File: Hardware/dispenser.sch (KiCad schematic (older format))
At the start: 5 parts

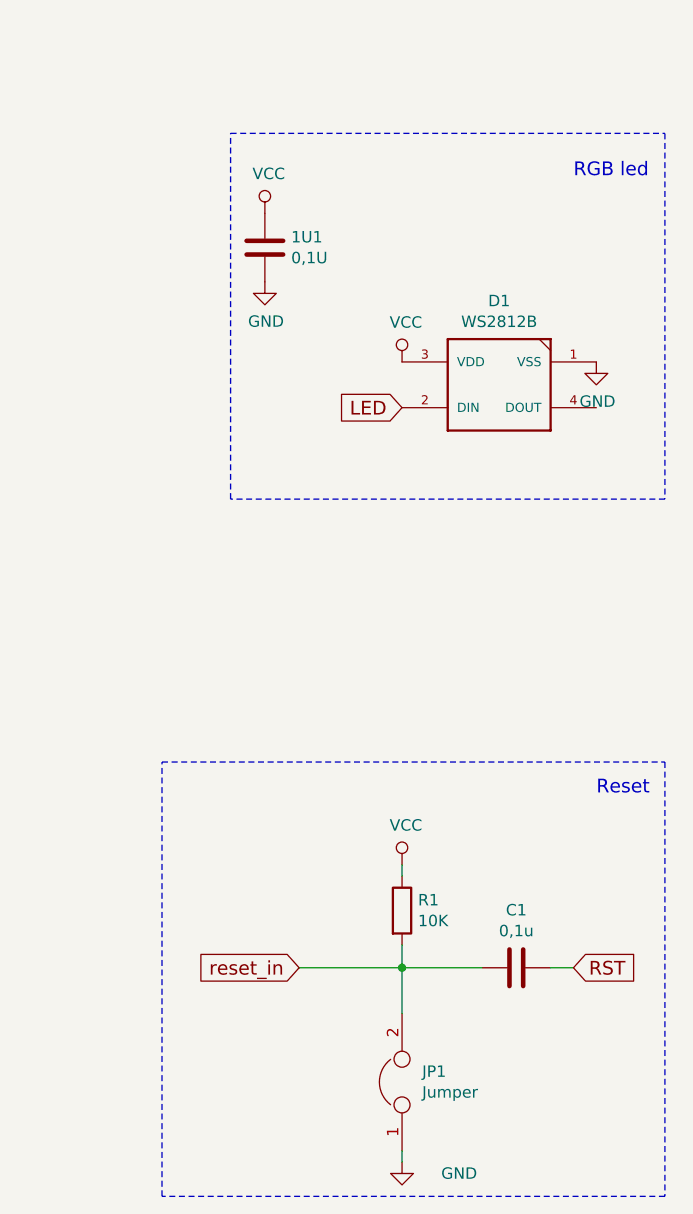
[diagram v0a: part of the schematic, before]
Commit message: one motor
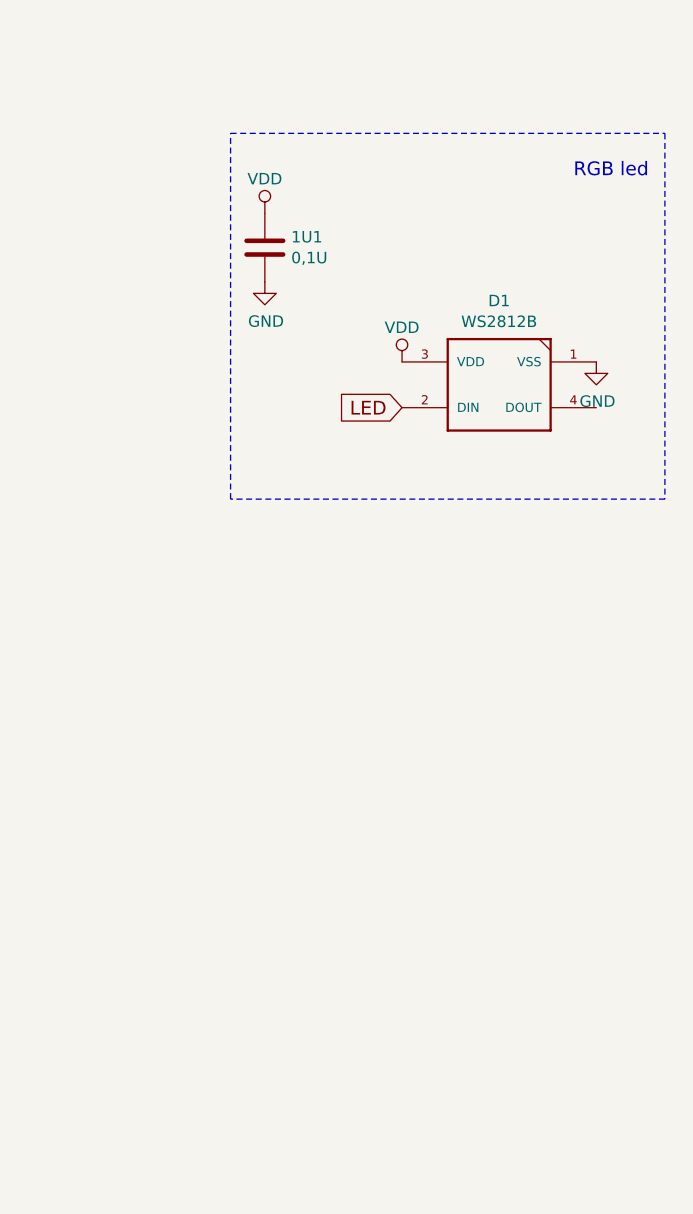
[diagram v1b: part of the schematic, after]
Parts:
- removed C1: 0,1u, Capacitors_SMD:C_0805_HandSoldering, symbol C
- removed JP1: Jumper, Pin_Headers:Pin_Header_Straight_1x03_Pitch2.54mm, symbol Jumper
- removed R1: 10K, Resistors_SMD:R_0805_HandSoldering, symbol R
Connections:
- net VCC renamed VDD
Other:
- note removed: "Reset\n"
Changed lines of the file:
@@
 Comment4 ""
 $EndDescr
-$Comp
-L C C1
-U 1 1 5A0702DF
-P 10200 5400
-F 0 "C1" V 9948 5400 50  0000 C CNN
-F 1 "0,1u" V 10039 5400 50  0000 C CNN
-F 2 "Capacitors_SMD:C_0805_HandSoldering" H 10238 5250 50  0001 C CNN
-F 3 "" H 10200 5400 50  0001 C CNN
-	1    10200 5400
-	0    1    1    0
-$EndComp
-Text GLabel 10450 5400 2    60   Input ~ 0
-RST
-$Comp
-L R R1
-U 1 1 5A0702E1
-P 9700 5150
-F 0 "R1" H 9770 5196 50  0000 L CNN
-F 1 "10K" H 9770 5105 50  0000 L CNN
-F 2 "Resistors_SMD:R_0805_HandSoldering" V 9630 5150 50  0001 C CNN
-F 3 "" H 9700 5150 50  0001 C CNN
-	1    9700 5150
-	1    0    0    -1
-$EndComp
-$Comp
-L VCC #PWR01
-U 1 1 5A0702E2
-P 9700 4950
-F 0 "#PWR01" H 9700 4800 50  0001 C CNN
-F 1 "VCC" H 9717 5123 50  0000 C CNN
-F 2 "" H 9700 4950 50  0001 C CNN
-F 3 "" H 9700 4950 50  0001 C CNN
-	1    9700 4950
-	1    0    0    -1
-$EndComp
-$Comp
-L GND #PWR02
-U 1 1 5A0702E3
-P 9700 6250
-F 0 "#PWR02" H 9700 6000 50  0001 C CNN
-F 1 "GND" H 9950 6200 50  0000 C CNN
-F 2 "" H 9700 6250 50  0001 C CNN
-F 3 "" H 9700 6250 50  0001 C CNN
-	1    9700 6250
-	1    0    0    -1
-$EndComp
-$Comp
-L VCC #PWR03
-U 1 1 5A0702ED
-P 9700 2750
-F 0 "#PWR03" H 9700 2600 50  0001 C CNN
-F 1 "VCC" H 9717 2923 50  0000 C CNN
-F 2 "" H 9700 2750 50  0001 C CNN
-F 3 "" H 9700 2750 50  0001 C CNN
-	1    9700 2750
-	1    0    0    -1
-$EndComp
-$Comp
-L Jumper JP1
-U 1 1 5A070E88
-P 9700 5900
-F 0 "JP1" V 9746 5812 50  0000 R CNN
-F 1 "Jumper" V 9655 5812 50  0000 R CNN
-F 2 "Pin_Headers:Pin_Header_Straight_1x03_Pitch2.54mm" H 9700 5900 50  0001 C CNN
-F 3 "" H 9700 5900 50  0001 C CNN
-	1    9700 5900
-	0    -1   -1   0
-$EndComp
-Text GLabel 9250 5400 0    60   Input ~ 0
-reset_in
-Text Notes 10550 4650 0    60   ~ 0
-Reset\n
 Text Notes 10450 1950 0    60   ~ 0
 RGB led
-Wire Wire Line
-	9250 5400 10050 5400
-Wire Wire Line
-	9700 5300 9700 5600
-Connection ~ 9700 5400
-Wire Wire Line
-	9700 5000 9700 4950
 Wire Notes Line
 	8950 1750 10850 1750
@@
 Wire Notes Line
 	8950 3350 8950 1750
-Wire Wire Line
-	10350 5400 10450 5400
-Wire Wire Line
-	9700 6250 9700 6200
-Wire Notes Line
-	8650 4500 10850 4500
-Wire Notes Line
-	10850 4500 10850 6400
-Wire Notes Line
-	10850 6400 8650 6400
-Wire Notes Line
-	8650 6400 8650 4500
 $Comp
 L C 1U1
@@
 $EndComp
 $Comp
-L VCC #PWR04
-U 1 1 5A0864F6
-P 9100 2100
-F 0 "#PWR04" H 9100 1950 50  0001 C CNN
-F 1 "VCC" H 9117 2273 50  0000 C CNN
-F 2 "" H 9100 2100 50  0001 C CNN
-F 3 "" H 9100 2100 50  0001 C CNN
-	1    9100 2100
-	1    0    0    -1
-$EndComp
-$Comp
-L GND #PWR05
+L GND #PWR03
 U 1 1 5A0864FC
 P 9100 2400
-F 0 "#PWR05" H 9100 2150 50  0001 C CNN
+F 0 "#PWR03" H 9100 2150 50  0001 C CNN
 F 1 "GND" H 9105 2227 50  0000 C CNN
 F 2 "" H 9100 2400 50  0001 C CNN
@@
 $EndComp
 $Comp
-L GND #PWR06
+L GND #PWR04
 U 1 1 5A08A0E4
 P 10550 2750
-F 0 "#PWR06" H 10550 2500 50  0001 C CNN
+F 0 "#PWR04" H 10550 2500 50  0001 C CNN
 F 1 "GND" H 10555 2577 50  0000 C CNN
 F 2 "" H 10550 2750 50  0001 C CNN
@@
 Text Notes 4800 4750 0    60   ~ 0
 Inputs
+$Comp
+L VDD #PWR05
+U 1 1 5AAFCA42
+P 9100 2100
+F 0 "#PWR05" H 9100 1950 50  0001 C CNN
+F 1 "VDD" H 9100 2250 50  0000 C CNN
+F 2 "" H 9100 2100 50  0001 C CNN
+F 3 "" H 9100 2100 50  0001 C CNN
+	1    9100 2100
+	1    0    0    -1
+$EndComp
+$Comp
+L VDD #PWR06
+U 1 1 5AAFCA63
+P 9700 2750
+F 0 "#PWR06" H 9700 2600 50  0001 C CNN
+F 1 "VDD" H 9700 2900 50  0000 C CNN
+F 2 "" H 9700 2750 50  0001 C CNN
+F 3 "" H 9700 2750 50  0001 C CNN
+	1    9700 2750
+	1    0    0    -1
+$EndComp
 $EndSCHEMATC
